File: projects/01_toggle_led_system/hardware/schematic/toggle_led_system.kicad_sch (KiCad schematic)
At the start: 5 parts, among them SW2 SW_MEC_5E

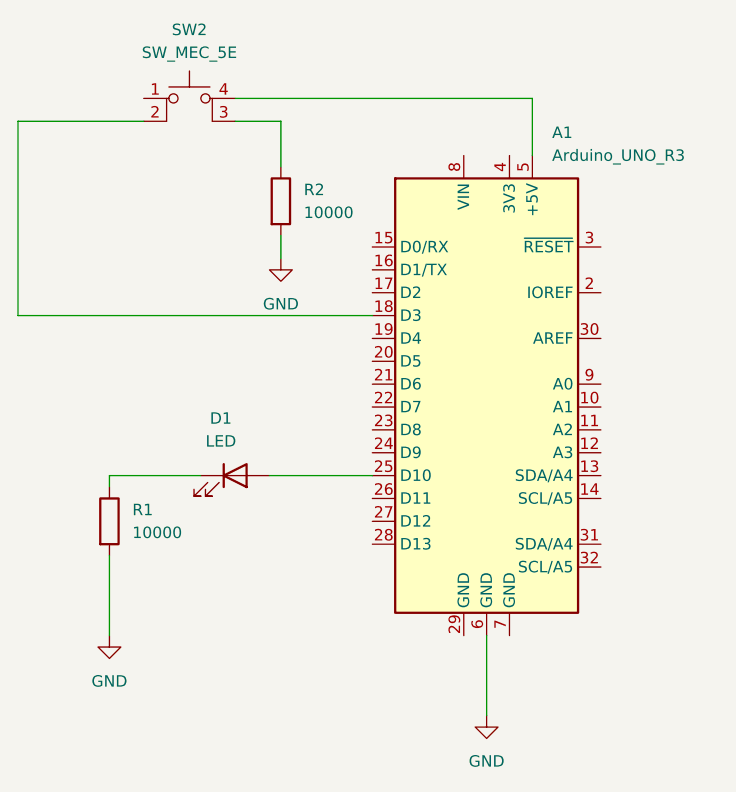
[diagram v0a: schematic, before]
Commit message: refactor(hardware): update resistor values in circuit schemma
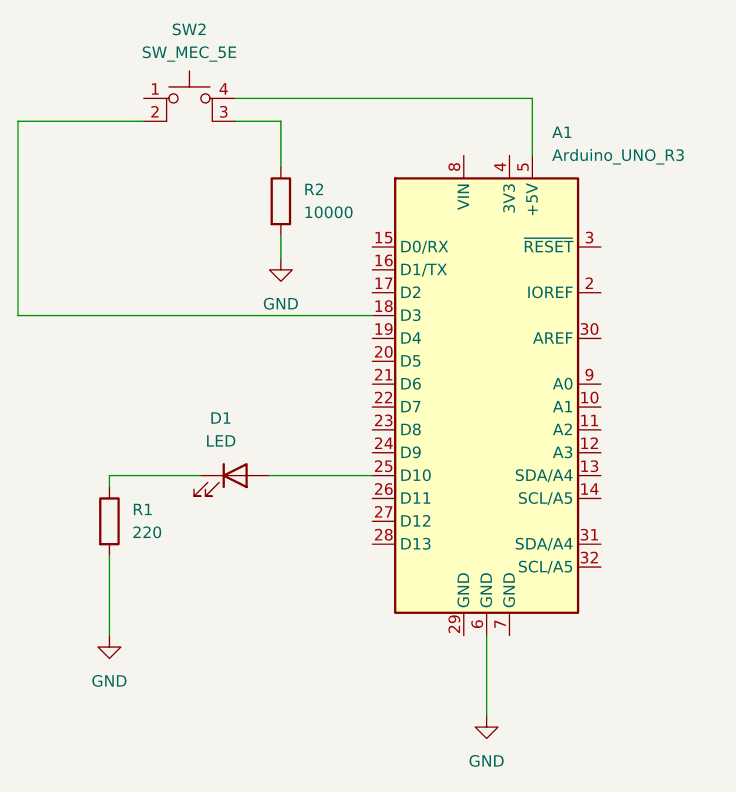
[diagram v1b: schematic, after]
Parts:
- R1: value 10000 -> 220
